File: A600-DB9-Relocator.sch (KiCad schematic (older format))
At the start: 3 parts, among them J1 DB9_Female, J2 DB9_Female, J3 DB9-Dual-Male

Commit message: PCB complete
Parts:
- added J4, J5: Conn_02x09_Odd_Even, Connector_PinHeader_2.54mm:PinHeader_2x09_P2.54mm_Vertical, symbol Connector_Generic:Conn_02x09_Odd_Even
- J1, J2: symbol Connector:DB9_Female -> A600-DB9-Relocator-rescue:DB9_Female-Connector
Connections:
- net at J3.A1: now also J5.1 (Pin_1); no longer J1.1
- net at J3.A2: now also J5.5 (Pin_5); no longer J1.2
- net at J3.A3: now also J5.9 (Pin_9); no longer J1.3
- net at J3.A4: now also J5.13 (Pin_13); no longer J1.4
- net at J3.A5: now also J5.17 (Pin_17); no longer J1.5
- net at J3.A6: now also J5.3 (Pin_3); no longer J1.6
- net at J3.A7: now also J5.7 (Pin_7); no longer J1.7
- net at J3.A8: now also J5.11 (Pin_11); no longer J1.8
- net at J3.A9: now also J5.15 (Pin_15); no longer J1.9
- net at J3.B1: now also J5.18 (Pin_18); no longer J2.1
- net at J3.B2: now also J5.14 (Pin_14); no longer J2.2
- net at J3.B3: now also J5.10 (Pin_10); no longer J2.3
- net at J3.B4: now also J5.6 (Pin_6); no longer J2.4
- net at J3.B5: now also J5.2 (Pin_2); no longer J2.5
- net at J3.B6: now also J5.16 (Pin_16); no longer J2.6
- net at J3.B7: now also J5.12 (Pin_12); no longer J2.7
- net at J3.B8: now also J5.8 (Pin_8); no longer J2.8
- net at J3.B9: now also J5.4 (Pin_4); no longer J2.9
- new net: J1.1, J4.17 (Pin_17)
- new net: J1.2, J4.13 (Pin_13)
- new net: J1.3, J4.9 (Pin_9)
- new net: J1.4, J4.5 (Pin_5)
- new net: J1.5, J4.1 (Pin_1)
- new net: J1.6, J4.15 (Pin_15)
- new net: J1.7, J4.11 (Pin_11)
- new net: J1.8, J4.7 (Pin_7)
- new net: J1.9, J4.3 (Pin_3)
- new net: J2.1, J4.2 (Pin_2)
- new net: J2.2, J4.6 (Pin_6)
- new net: J2.3, J4.10 (Pin_10)
- new net: J2.4, J4.14 (Pin_14)
- new net: J2.5, J4.18 (Pin_18)
- new net: J2.6, J4.4 (Pin_4)
- new net: J2.7, J4.8 (Pin_8)
- new net: J2.8, J4.12 (Pin_12)
- new net: J2.9, J4.16 (Pin_16)
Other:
- moved on the sheet: J3
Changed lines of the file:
@@
 L Dual-DB9:DB9-Dual-Male J3
 U 1 1 5EE3188A
-P 2750 5050
-F 0 "J3" H 2750 4777 50  0000 C CNN
-F 1 "DB9-Dual-Male" H 2750 4686 50  0000 C CNN
-F 2 "A600:CONN-DUAL-D-SUB-9POS-RA-SLDR" H 2750 5050 50  0001 C CNN
-F 3 "" H 2750 5050 50  0001 C CNN
-	1    2750 5050
+P 3150 6200
+F 0 "J3" H 3150 5927 50  0000 C CNN
+F 1 "DB9-Dual-Male" H 3150 5836 50  0000 C CNN
+F 2 "A600:CONN-DUAL-D-SUB-9POS-RA-SLDR" H 3150 6200 50  0001 C CNN
+F 3 "" H 3150 6200 50  0001 C CNN
+	1    3150 6200
 	1    0    0    -1
 $EndComp
 $Comp
-L Connector:DB9_Female J1
+L A600-DB9-Relocator-rescue:DB9_Female-Connector J1
 U 1 1 5EE33114
 P 2200 2425
@@
 $EndComp
 $Comp
-L Connector:DB9_Female J2
+L A600-DB9-Relocator-rescue:DB9_Female-Connector J2
 U 1 1 5EE370FC
 P 4125 2425
@@
 	0    -1   -1   0
 $EndComp
-Wire Wire Line
-	1800 2725 1800 4750
-Wire Wire Line
-	1900 2725 1900 4750
-Wire Wire Line
-	2000 2725 2000 4750
-Wire Wire Line
-	2100 2725 2100 4750
-Wire Wire Line
-	2200 2725 2200 4750
-Wire Wire Line
-	2300 2725 2300 4750
-Wire Wire Line
-	2400 2725 2400 4750
-Wire Wire Line
-	2500 2725 2500 4750
-Wire Wire Line
-	2600 2725 2600 4750
-Wire Wire Line
-	2900 4750 2900 3000
-Wire Wire Line
-	2900 3000 3725 3000
-Wire Wire Line
-	3725 3000 3725 2725
-Wire Wire Line
-	3000 4750 3000 3050
-Wire Wire Line
-	3000 3050 3825 3050
-Wire Wire Line
-	3825 3050 3825 2725
-Wire Wire Line
-	3100 4750 3100 3100
-Wire Wire Line
-	3100 3100 3925 3100
-Wire Wire Line
-	3925 3100 3925 2725
-Wire Wire Line
-	3200 4750 3200 3150
-Wire Wire Line
-	3200 3150 4025 3150
-Wire Wire Line
-	4025 3150 4025 2725
-Wire Wire Line
-	3300 4750 3300 3200
-Wire Wire Line
-	3300 3200 4125 3200
-Wire Wire Line
-	4125 3200 4125 2725
-Wire Wire Line
-	3400 4750 3400 3250
-Wire Wire Line
-	3400 3250 4225 3250
-Wire Wire Line
-	4225 3250 4225 2725
-Wire Wire Line
-	3500 4750 3500 3300
-Wire Wire Line
-	3500 3300 4325 3300
-Wire Wire Line
-	4325 3300 4325 2725
-Wire Wire Line
-	3600 4750 3600 3350
-Wire Wire Line
-	3600 3350 4425 3350
-Wire Wire Line
-	4425 3350 4425 2725
-Wire Wire Line
-	3700 4750 3700 3400
-Wire Wire Line
-	3700 3400 4525 3400
-Wire Wire Line
-	4525 3400 4525 2725
 Text Notes 7125 6775 0    50   ~ 0
 Relocate side-mounted A600 mouse & game ports to rear
@@
 Text Notes 8125 7650 0    50   ~ 0
 12 June 2020
+$Comp
+L Connector_Generic:Conn_02x09_Odd_Even J4
+U 1 1 5F743026
+P 3100 3550
+F 0 "J4" H 3150 4167 50  0000 C CNN
+F 1 "Conn_02x09_Odd_Even" H 3150 4076 50  0000 C CNN
+F 2 "Connector_PinHeader_2.54mm:PinHeader_2x09_P2.54mm_Vertical" H 3100 3550 50  0001 C CNN
+F 3 "~" H 3100 3550 50  0001 C CNN
+	1    3100 3550
+	1    0    0    -1
+$EndComp
+Wire Wire Line
+	3725 2725 3725 3150
+Wire Wire Line
+	3725 3150 3400 3150
+Wire Wire Line
+	3400 3250 3825 3250
+Wire Wire Line
+	3825 3250 3825 2725
+Wire Wire Line
+	3925 2725 3925 3350
+Wire Wire Line
+	3925 3350 3400 3350
+Wire Wire Line
+	4025 2725 4025 3450
+Wire Wire Line
+	4025 3450 3400 3450
+Wire Wire Line
+	4125 2725 4125 3550
+Wire Wire Line
+	4125 3550 3400 3550
+Wire Wire Line
+	4225 2725 4225 3650
+Wire Wire Line
+	4225 3650 3400 3650
+Wire Wire Line
+	4325 2725 4325 3750
+Wire Wire Line
+	4325 3750 3400 3750
+Wire Wire Line
+	4425 2725 4425 3850
+Wire Wire Line
+	4425 3850 3400 3850
+Wire Wire Line
+	4525 2725 4525 3950
+Wire Wire Line
+	4525 3950 3400 3950
+Wire Wire Line
+	2900 3150 2600 3150
+Wire Wire Line
+	2600 3150 2600 2725
+Wire Wire Line
+	2900 3250 2500 3250
+Wire Wire Line
+	2500 3250 2500 2725
+Wire Wire Line
+	2900 3350 2400 3350
+Wire Wire Line
+	2400 3350 2400 2725
+Wire Wire Line
+	2900 3450 2300 3450
+Wire Wire Line
+	2300 3450 2300 2725
+Wire Wire Line
+	2200 2725 2200 3550
+Wire Wire Line
+	2200 3550 2900 3550
+Wire Wire Line
+	2100 2725 2100 3650
+Wire Wire Line
+	2100 3650 2900 3650
+Wire Wire Line
+	2000 2725 2000 3750
+Wire Wire Line
+	2000 3750 2900 3750
+Wire Wire Line
+	1900 2725 1900 3850
+Wire Wire Line
+	1900 3850 2900 3850
+Wire Wire Line
+	1800 2725 1800 3950
+Wire Wire Line
+	1800 3950 2900 3950
+$Comp
+L Connector_Generic:Conn_02x09_Odd_Even J5
+U 1 1 5F74A4B2
+P 3100 4850
+F 0 "J5" H 3150 5467 50  0000 C CNN
+F 1 "Conn_02x09_Odd_Even" H 3150 5376 50  0000 C CNN
+F 2 "Connector_PinHeader_2.54mm:PinHeader_2x09_P2.54mm_Vertical" H 3100 4850 50  0001 C CNN
+F 3 "~" H 3100 4850 50  0001 C CNN
+	1    3100 4850
+	1    0    0    -1
+$EndComp
+Wire Wire Line
+	2900 4450 2200 4450
+Wire Wire Line
+	2200 4450 2200 5900
+Wire Wire Line
+	2300 5900 2300 4550
+Wire Wire Line
+	2300 4550 2900 4550
+Wire Wire Line
+	2400 5900 2400 4650
+Wire Wire Line
+	2400 4650 2900 4650
+Wire Wire Line
+	2500 5900 2500 4750
+Wire Wire Line
+	2500 4750 2900 4750
+Wire Wire Line
+	2900 4850 2600 4850
+Wire Wire Line
+	2600 4850 2600 5900
+Wire Wire Line
+	2900 4950 2700 4950
+Wire Wire Line
+	2700 4950 2700 5900
+Wire Wire Line
+	2900 5050 2800 5050
+Wire Wire Line
+	2800 5050 2800 5900
+Wire Wire Line
+	3000 5900 3000 5300
+Wire Wire Line
+	3000 5300 2900 5300
+Wire Wire Line
+	2900 5300 2900 5250
+Wire Wire Line
+	2900 5325 2850 5325
+Wire Wire Line
+	2850 5325 2850 5150
+Wire Wire Line
+	2850 5150 2900 5150
+Wire Wire Line
+	2900 5325 2900 5900
+Wire Wire Line
+	3400 5250 3400 5300
+Wire Wire Line
+	3400 5300 3300 5300
+Wire Wire Line
+	3300 5300 3300 5900
+Wire Wire Line
+	3400 5900 3400 5325
+Wire Wire Line
+	3400 5325 3450 5325
+Wire Wire Line
+	3450 5325 3450 5150
+Wire Wire Line
+	3450 5150 3400 5150
+Wire Wire Line
+	3400 5050 3500 5050
+Wire Wire Line
+	3500 5050 3500 5900
+Wire Wire Line
+	3400 4950 3600 4950
+Wire Wire Line
+	3600 4950 3600 5900
+Wire Wire Line
+	3400 4850 3700 4850
+Wire Wire Line
+	3700 4850 3700 5900
+Wire Wire Line
+	3400 4750 3800 4750
+Wire Wire Line
+	3800 4750 3800 5900
+Wire Wire Line
+	3400 4650 3900 4650
+Wire Wire Line
+	3900 4650 3900 5900
+Wire Wire Line
+	3400 4550 4000 4550
+Wire Wire Line
+	4000 4550 4000 5900
+Wire Wire Line
+	3400 4450 4100 4450
+Wire Wire Line
+	4100 4450 4100 5900
 $EndSCHEMATC

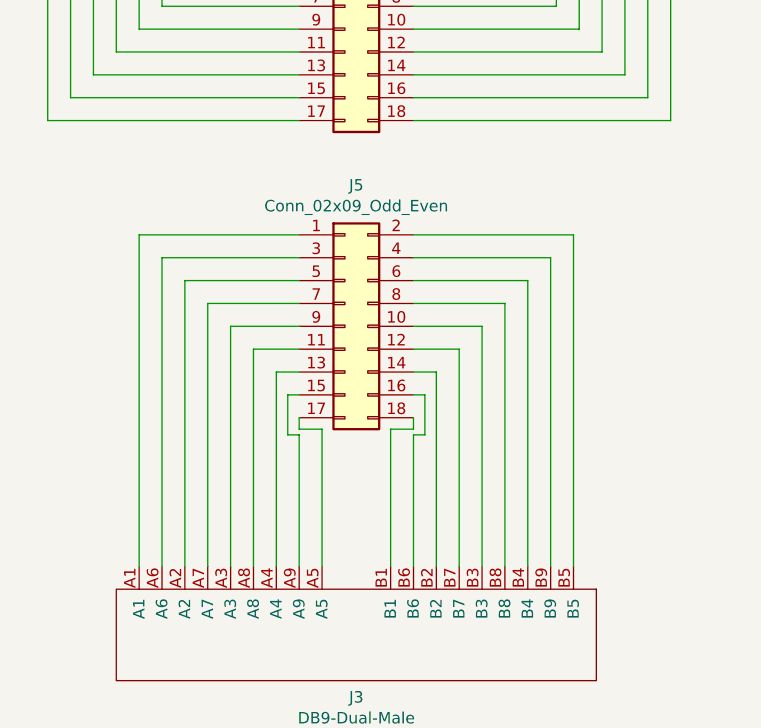
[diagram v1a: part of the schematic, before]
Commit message: Corrected routing; title block
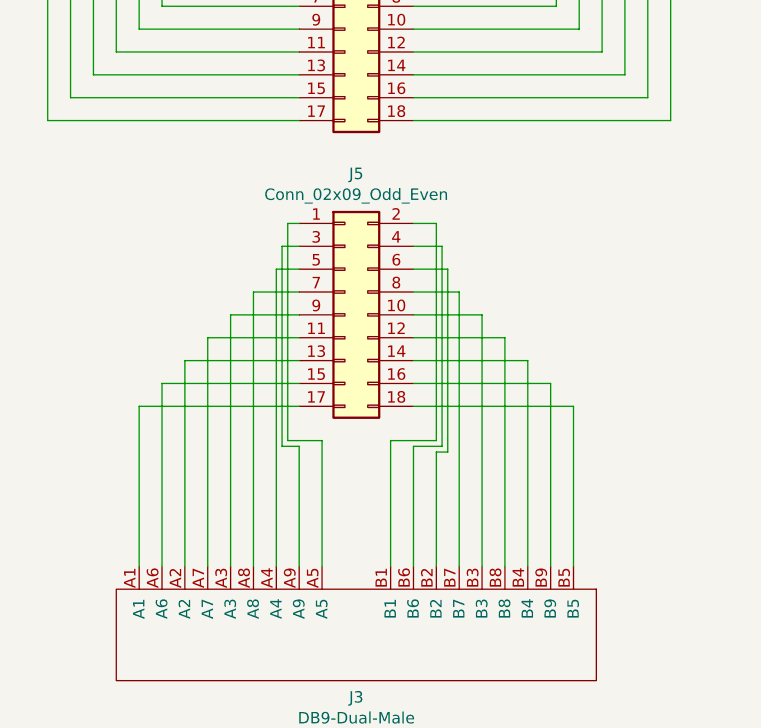
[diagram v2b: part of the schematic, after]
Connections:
- net at J3.A1: now also J5.17 (Pin_17); no longer J5.1 (Pin_1)
- net at J3.A2: now also J5.13 (Pin_13); no longer J5.5 (Pin_5)
- net at J3.A4: now also J5.5 (Pin_5); no longer J5.13 (Pin_13)
- net at J3.A5: now also J5.1 (Pin_1); no longer J5.17 (Pin_17)
- net at J3.A6: now also J5.15 (Pin_15); no longer J5.3 (Pin_3)
- net at J3.A7: now also J5.11 (Pin_11); no longer J5.7 (Pin_7)
- net at J3.A8: now also J5.7 (Pin_7); no longer J5.11 (Pin_11)
- net at J3.A9: now also J5.3 (Pin_3); no longer J5.15 (Pin_15)
- net at J3.B1: now also J5.2 (Pin_2); no longer J5.18 (Pin_18)
- net at J3.B2: now also J5.6 (Pin_6); no longer J5.14 (Pin_14)
- net at J3.B4: now also J5.14 (Pin_14); no longer J5.6 (Pin_6)
- net at J3.B5: now also J5.18 (Pin_18); no longer J5.2 (Pin_2)
- net at J3.B6: now also J5.4 (Pin_4); no longer J5.16 (Pin_16)
- net at J3.B7: now also J5.8 (Pin_8); no longer J5.12 (Pin_12)
- net at J3.B8: now also J5.12 (Pin_12); no longer J5.8 (Pin_8)
- net at J3.B9: now also J5.16 (Pin_16); no longer J5.4 (Pin_4)
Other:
- moved on the sheet: J5
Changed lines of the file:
@@
 L Connector_Generic:Conn_02x09_Odd_Even J5
 U 1 1 5F74A4B2
-P 3100 4850
-F 0 "J5" H 3150 5467 50  0000 C CNN
-F 1 "Conn_02x09_Odd_Even" H 3150 5376 50  0000 C CNN
-F 2 "Connector_PinHeader_2.54mm:PinHeader_2x09_P2.54mm_Vertical" H 3100 4850 50  0001 C CNN
-F 3 "~" H 3100 4850 50  0001 C CNN
-	1    3100 4850
+P 3100 4800
+F 0 "J5" H 3150 5417 50  0000 C CNN
+F 1 "Conn_02x09_Odd_Even" H 3150 5326 50  0000 C CNN
+F 2 "Connector_PinHeader_2.54mm:PinHeader_2x09_P2.54mm_Vertical" H 3100 4800 50  0001 C CNN
+F 3 "~" H 3100 4800 50  0001 C CNN
+	1    3100 4800
 	1    0    0    -1
 $EndComp
 Wire Wire Line
-	2900 4450 2200 4450
+	2900 5200 2200 5200
 Wire Wire Line
-	2200 4450 2200 5900
+	2200 5200 2200 5900
 Wire Wire Line
-	2300 5900 2300 4550
+	2900 5100 2300 5100
 Wire Wire Line
-	2300 4550 2900 4550
+	2300 5100 2300 5900
 Wire Wire Line
-	2400 5900 2400 4650
+	2900 5000 2400 5000
 Wire Wire Line
-	2400 4650 2900 4650
+	2400 5000 2400 5900
 Wire Wire Line
-	2500 5900 2500 4750
+	2900 4900 2500 4900
 Wire Wire Line
-	2500 4750 2900 4750
+	2500 4900 2500 5900
 Wire Wire Line
-	2900 4850 2600 4850
+	3000 5900 3000 5350
 Wire Wire Line
-	2600 4850 2600 5900
+	3000 5350 2850 5350
 Wire Wire Line
-	2900 4950 2700 4950
+	2850 5350 2850 4400
 Wire Wire Line
-	2700 4950 2700 5900
+	2850 4400 2900 4400
 Wire Wire Line
-	2900 5050 2800 5050
+	2900 5900 2900 5375
 Wire Wire Line
-	2800 5050 2800 5900
+	2900 5375 2825 5375
 Wire Wire Line
-	3000 5900 3000 5300
+	2825 5375 2825 4500
 Wire Wire Line
-	3000 5300 2900 5300
+	2825 4500 2900 4500
 Wire Wire Line
-	2900 5300 2900 5250
+	2800 5900 2800 4600
 Wire Wire Line
-	2900 5325 2850 5325
+	2800 4600 2900 4600
 Wire Wire Line
-	2850 5325 2850 5150
+	2700 5900 2700 4700
 Wire Wire Line
-	2850 5150 2900 5150
+	2700 4700 2900 4700
 Wire Wire Line
-	2900 5325 2900 5900
+	2900 4800 2600 4800
 Wire Wire Line
-	3400 5250 3400 5300
+	2600 4800 2600 5900
 Wire Wire Line
-	3400 5300 3300 5300
+	3300 5900 3300 5350
 Wire Wire Line
-	3300 5300 3300 5900
+	3300 5350 3500 5350
 Wire Wire Line
-	3400 5900 3400 5325
+	3500 5350 3500 4400
 Wire Wire Line
-	3400 5325 3450 5325
+	3500 4400 3400 4400
 Wire Wire Line
-	3450 5325 3450 5150
+	3400 4500 3525 4500
 Wire Wire Line
-	3450 5150 3400 5150
+	3525 4500 3525 5375
 Wire Wire Line
-	3400 5050 3500 5050
+	3525 5375 3400 5375
 Wire Wire Line
-	3500 5050 3500 5900
+	3400 5375 3400 5900
 Wire Wire Line
-	3400 4950 3600 4950
+	3500 5900 3500 5400
 Wire Wire Line
-	3600 4950 3600 5900
+	3500 5400 3550 5400
 Wire Wire Line
-	3400 4850 3700 4850
+	3550 5400 3550 4600
 Wire Wire Line
-	3700 4850 3700 5900
+	3550 4600 3400 4600
 Wire Wire Line
-	3400 4750 3800 4750
+	3400 4700 3600 4700
 Wire Wire Line
-	3800 4750 3800 5900
+	3600 4700 3600 5900
 Wire Wire Line
-	3400 4650 3900 4650
+	3700 5900 3700 4800
 Wire Wire Line
-	3900 4650 3900 5900
+	3700 4800 3400 4800
 Wire Wire Line
-	3400 4550 4000 4550
+	3400 4900 3800 4900
 Wire Wire Line
-	4000 4550 4000 5900
+	3800 4900 3800 5900
 Wire Wire Line
-	3400 4450 4100 4450
+	3400 5000 3900 5000
 Wire Wire Line
-	4100 4450 4100 5900
+	3900 5000 3900 5900
+Wire Wire Line
+	3400 5100 4000 5100
+Wire Wire Line
+	4000 5100 4000 5900
+Wire Wire Line
+	3400 5200 4100 5200
+Wire Wire Line
+	4100 5200 4100 5900
 $EndSCHEMATC
